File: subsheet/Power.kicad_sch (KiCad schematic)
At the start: 35 parts, among them J501 Barrel_Jack, J502 PWR_IN, J503 ALTERNATE, Q501 DTC114E, Q502 DTC114E, U501 TPS2552DBV, U502 TPS2552DBV, U503 P331AWG-7

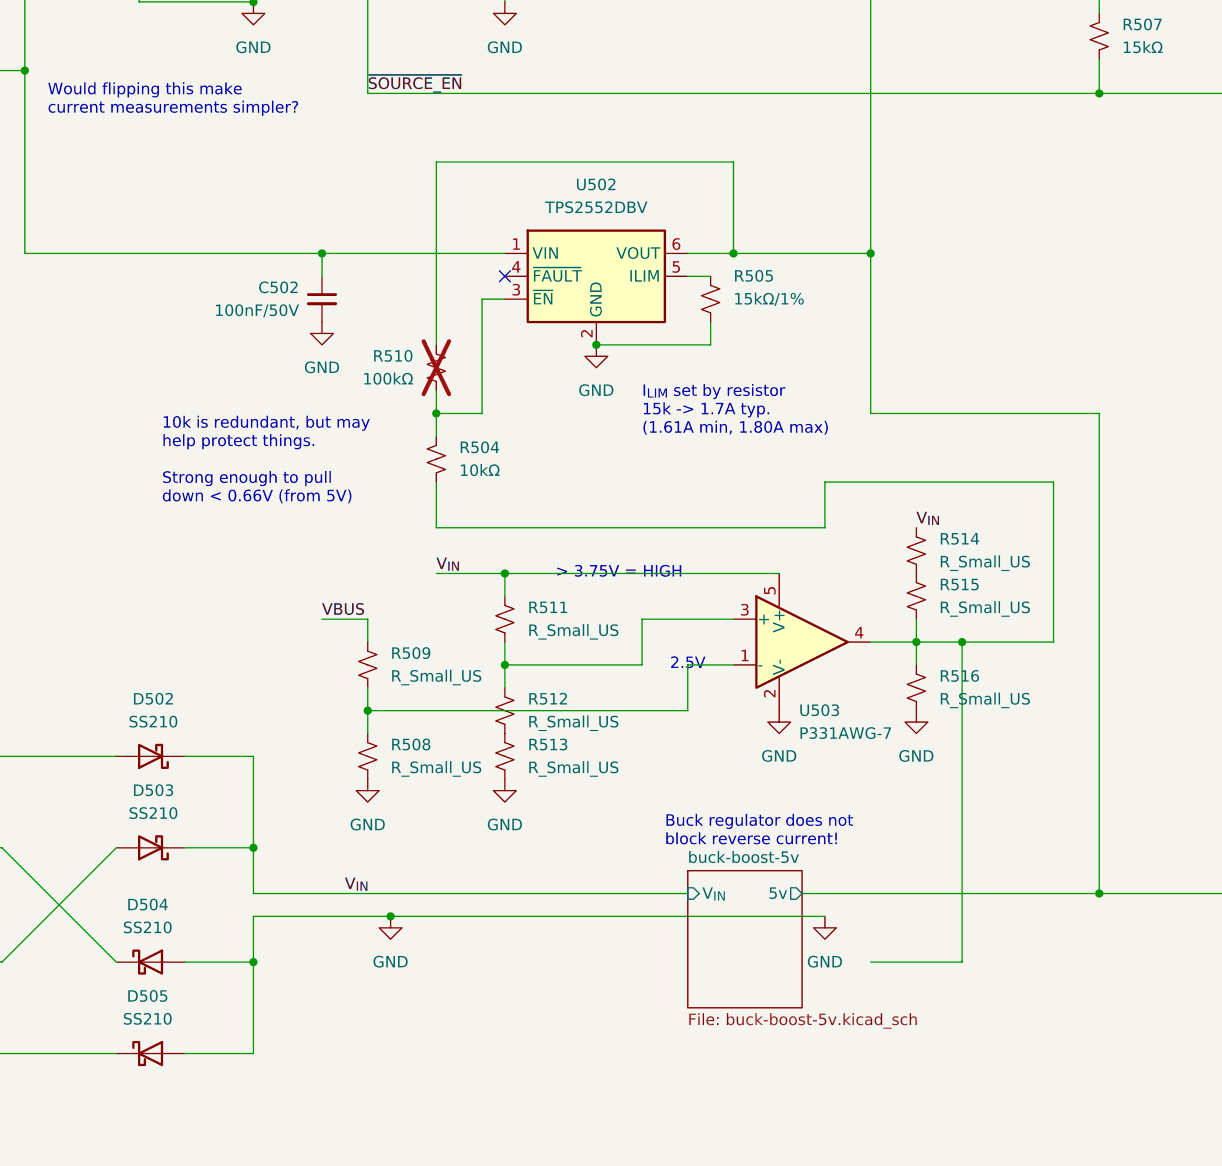
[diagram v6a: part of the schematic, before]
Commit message: Removed complex OR'ing circuit
Replaced it with a simple one that will turn off the USB 5V switch when
the buck-regulator is providing power (using PGOOD pin to signal this).

May not even be necessary, but good to have.
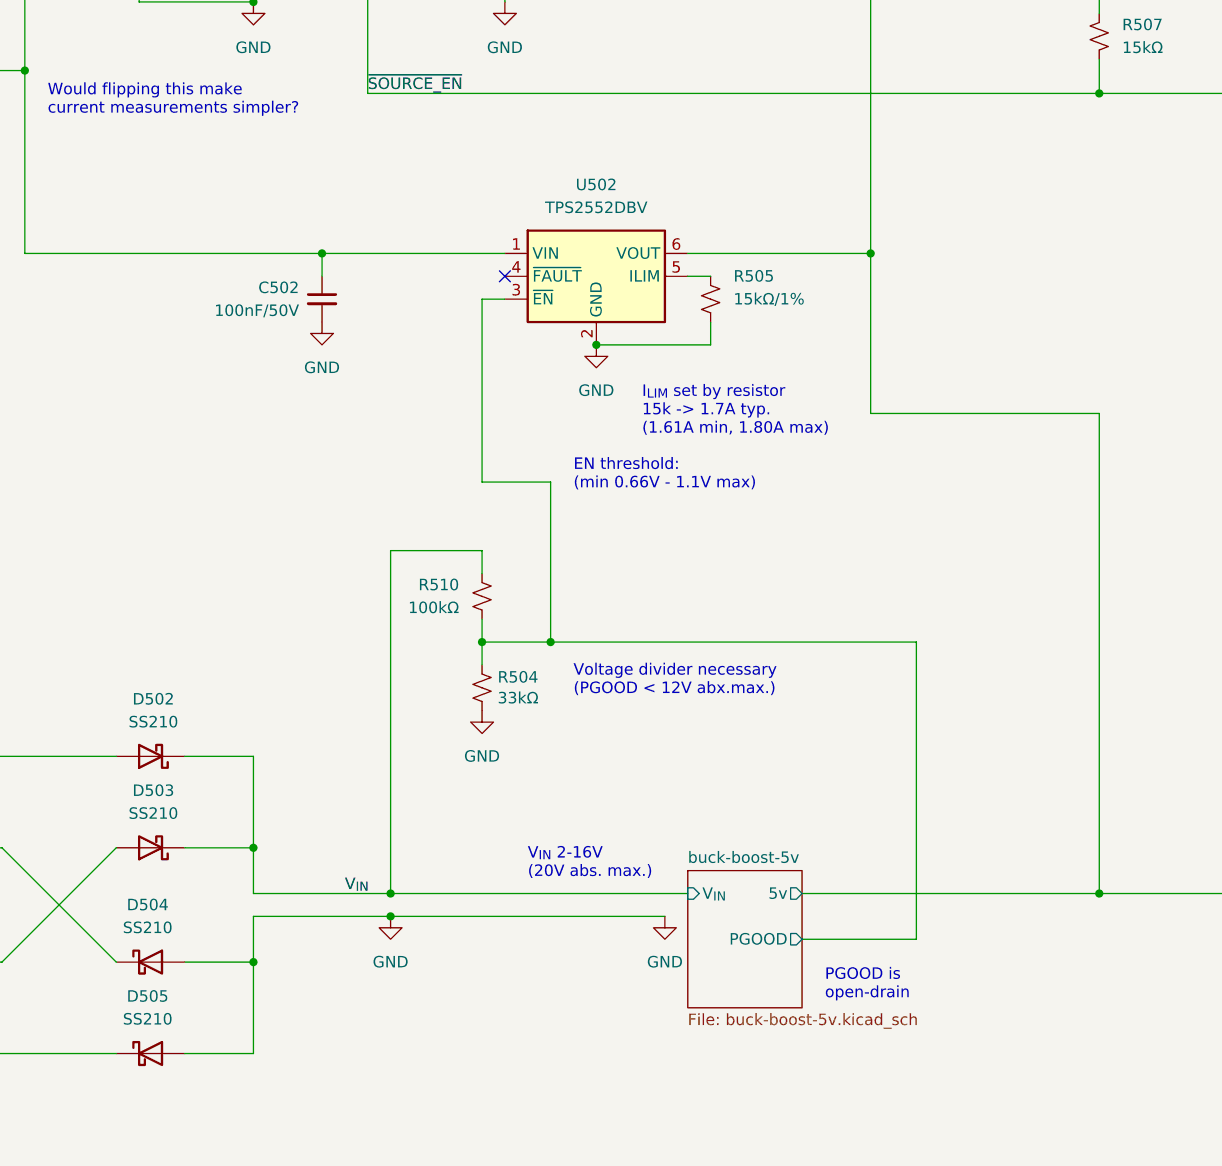
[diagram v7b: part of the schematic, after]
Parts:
- removed R508, R509, R511, R512, R513, R514, R515, R516: R_Small_US, symbol Device:R_Small_US
- removed U503: P331AWG-7, Package_TO_SOT_SMD:SOT-23-5, symbol Comparator:TL331
- R504: value 10kΩ -> 33kΩ; LCSC C25804 -> C4216
- R510: now fitted; now in the parts list
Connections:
- net +5V: no longer R510.1
- net GND: now also R504.2
- net V_{IN}: now also R510.1
- net buck-boost-5v/PGOOD: now reaches R504.1, R510.2, U502.3 (~{EN})
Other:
- sheet buck-boost-5v ports: added PGOOD; removed none
- note added: "EN threshold: (min 0.66V - 1.1V max)"
- note added: "PGOOD is open-drain"
- note added: "V_{IN} 2-16V (20V abs. max.)"
- note added: "Voltage divider necessary (PGOOD < 12V abx.max.)"
- note removed: "10k is redundant, but may help protect things. Strong enough to pull down < 0.66V (from 5V)"
- note removed: "2.5V"
- note removed: "> 3.75V = HIGH"
- note removed: "Buck regulator does not block reverse current!"

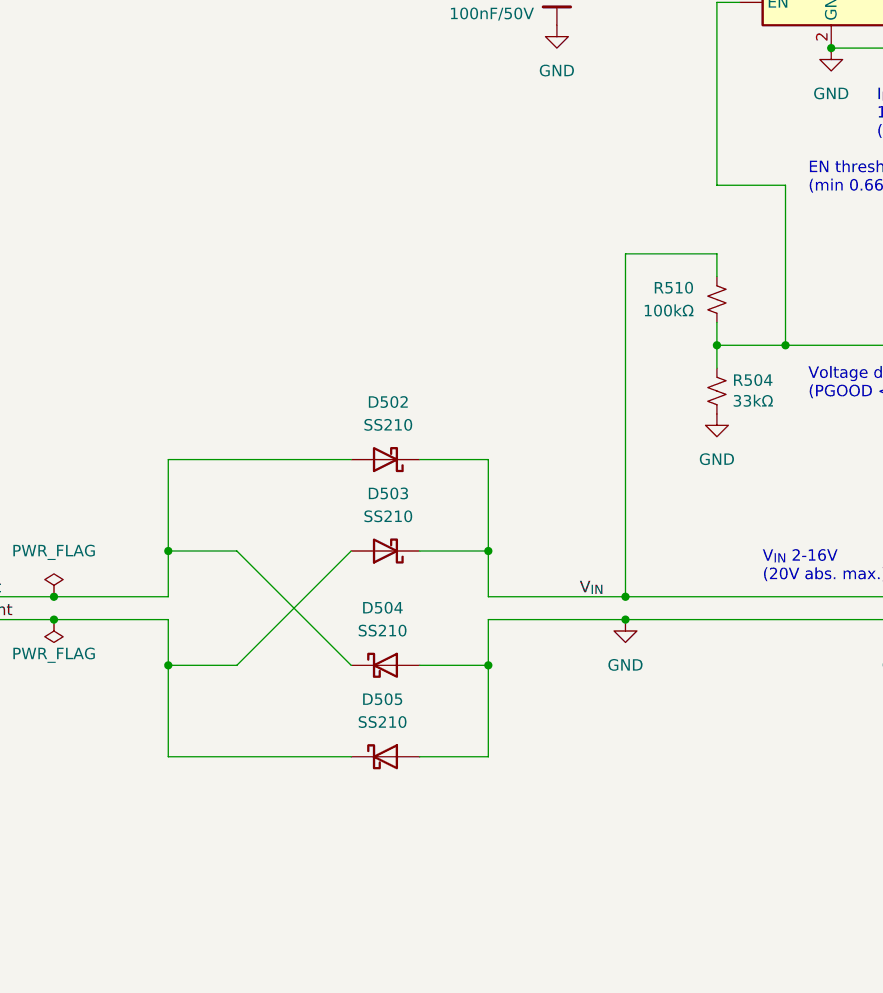
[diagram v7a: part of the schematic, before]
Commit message: Arranged buck-boost regulator. Moved some components slightly.
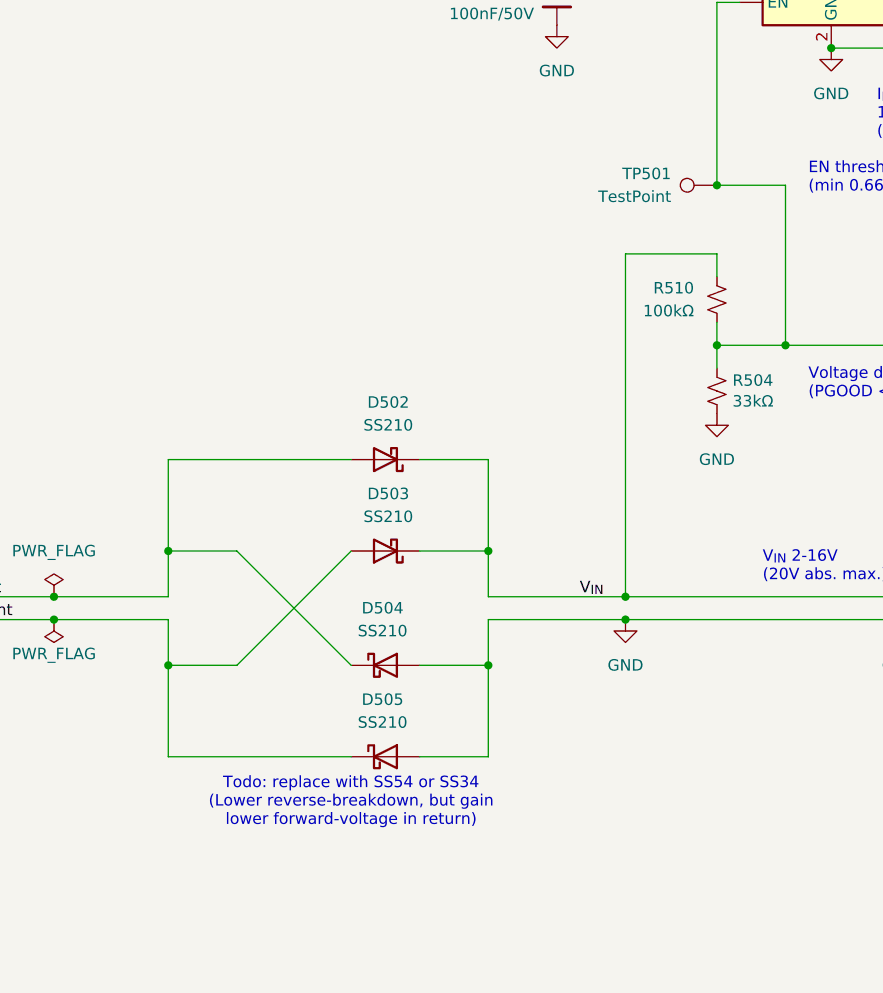
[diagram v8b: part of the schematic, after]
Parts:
- added TP501: TestPoint, symbol Connector:TestPoint
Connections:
- net buck-boost-5v/PGOOD: now also TP501.1
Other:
- note added: "Todo: replace with SS54 or SS34 (Lower reverse-breakdown, but gain lower forward-voltage in return)"
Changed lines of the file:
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@@
+	)
+	(junction
+		(at 121.92 86.36)
+		(diameter 0)
+		(color 0 0 0 0)
 	)
 	(junction
@@
 			)
 			(justify left bottom)
+		)
+	)
+	(text "Todo: replace with SS54 or SS34\n(Lower reverse-breakdown, but gain\nlower forward-voltage in return)"
+		(exclude_from_sim no)
+		(at 81.28 154.94 0)
+		(effects
+			(font
+				(size 1.27 1.27)
+			)
 		)
 	)
@@
 					(unit 1)
 				)
+			)
+		)
+	)
+	(symbol
+		(lib_id "Connector:TestPoint")
+		(at 121.92 86.36 90)
+		(unit 1)
+		(exclude_from_sim no)
+		(in_bom yes)
+		(on_board yes)
+		(dnp no)
+		(fields_autoplaced yes)
+		(property "Reference" "TP501"
+			(at 116.84 85.0899 90)
+			(effects
+				(font
+					(size 1.27 1.27)
+				)
+				(justify left)
+			)
+		)
+		(property "Value" "TestPoint"
+			(at 116.84 87.6299 90)
+			(effects
+				(font
+					(size 1.27 1.27)
+				)
+				(justify left)
+			)
+		)
+		(property "Footprint" ""
+			(at 121.92 81.28 0)
+			(effects
+				(font
+					(size 1.27 1.27)
+				)
+				(hide yes)
+			)
+		)
+		(property "Datasheet" "~"
+			(at 121.92 81.28 0)
+			(effects
+				(font
+					(size 1.27 1.27)
+				)
+				(hide yes)
+			)
+		)
+		(property "Description" "test point"
+			(at 121.92 86.36 0)
+			(effects
+				(font
+					(size 1.27 1.27)
+				)
+				(hide yes)
+			)
+		)
+		(pin "1"
+		)
+		(instances
+			(project "ESP_bare_chip_test_board"
+				(path "/45b6f84a-e69b-48be-a49b-bc68872e2c15/28425a28-8968-4679-b18b-58814452f93f"
+					(reference "TP501")
+					(unit 1)
+				)
